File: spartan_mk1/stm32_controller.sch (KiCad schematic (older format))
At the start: 26 parts

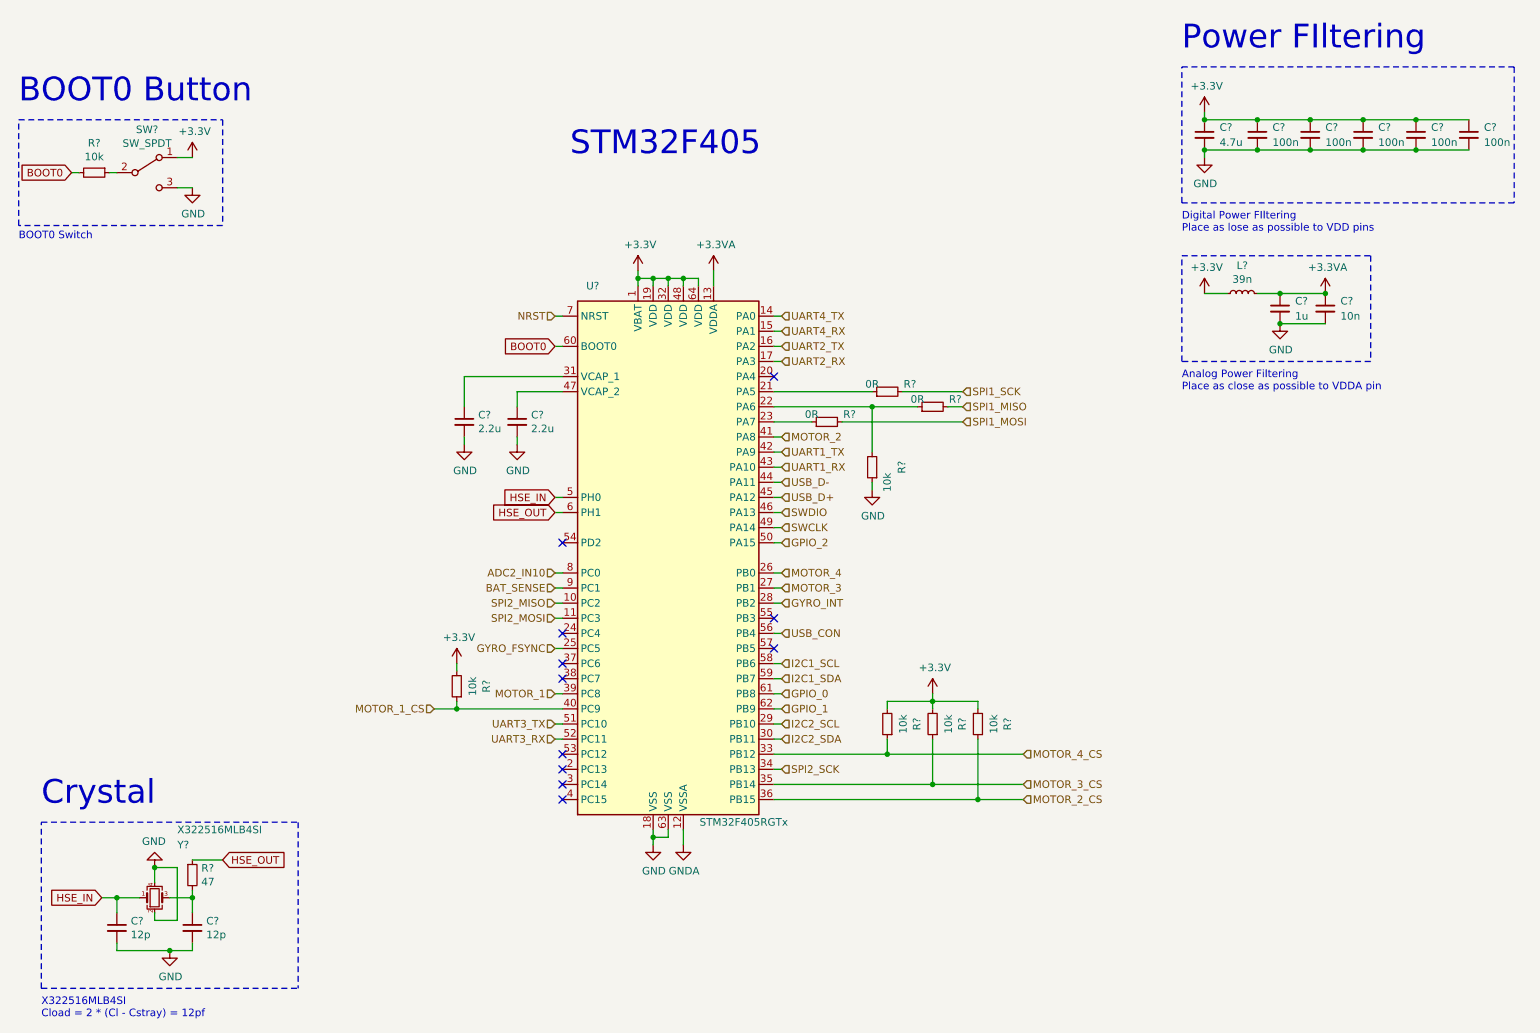
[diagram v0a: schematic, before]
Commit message: Complete schematic with DRC done
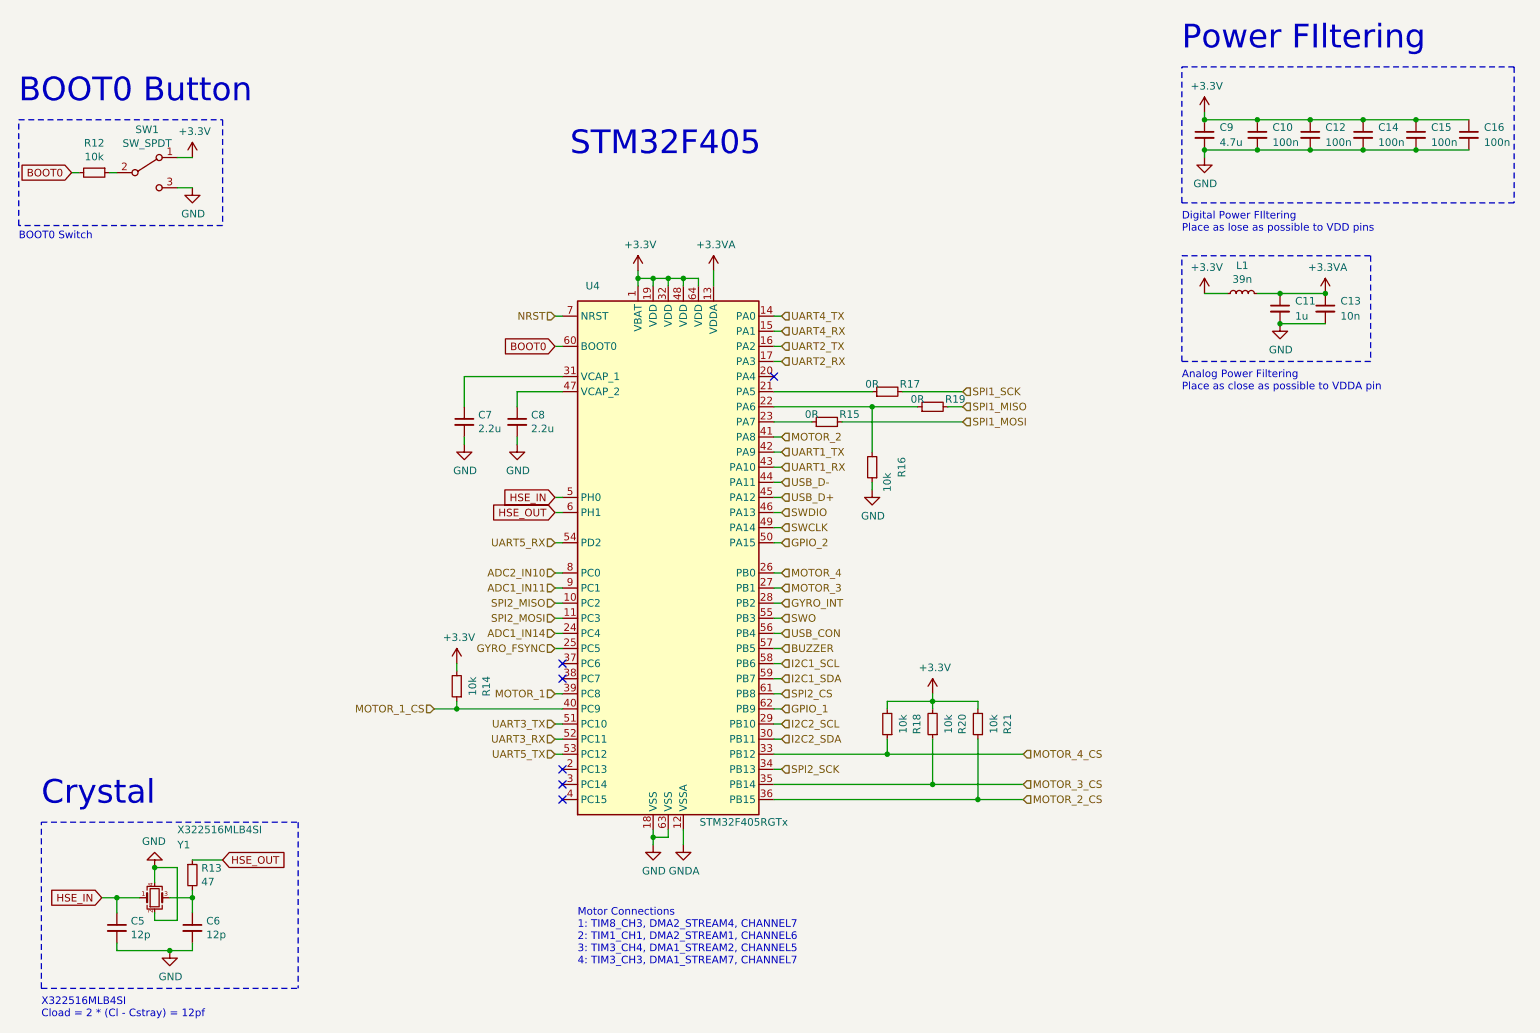
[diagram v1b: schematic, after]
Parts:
- gave numbers to parts that had none: 26
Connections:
- net ADC1_IN14: now reaches U4.24 (PC4)
- net UART5_TX: now reaches U4.53 (PC12)
- net UART5_RX: now reaches U4.54 (PD2)
- net SWO: now reaches U4.55 (PB3)
- net BUZZER: now reaches U4.57 (PB5)
- net BAT_SENSE renamed ADC1_IN11
- net GPIO_0 renamed SPI2_CS
- no-connect marks 11 -> 6
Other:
- note added: "Motor Connections\n1: TIM8_CH3, DMA2_STREAM4, CHANNEL7\n2: TIM1_CH1, DMA2_STREAM1, CHANNEL6\n3: TIM3_CH4, DMA1_STREAM2, CHANNEL5\n4: TIM3_CH3, DMA1_STREAM7, CHANNEL7"

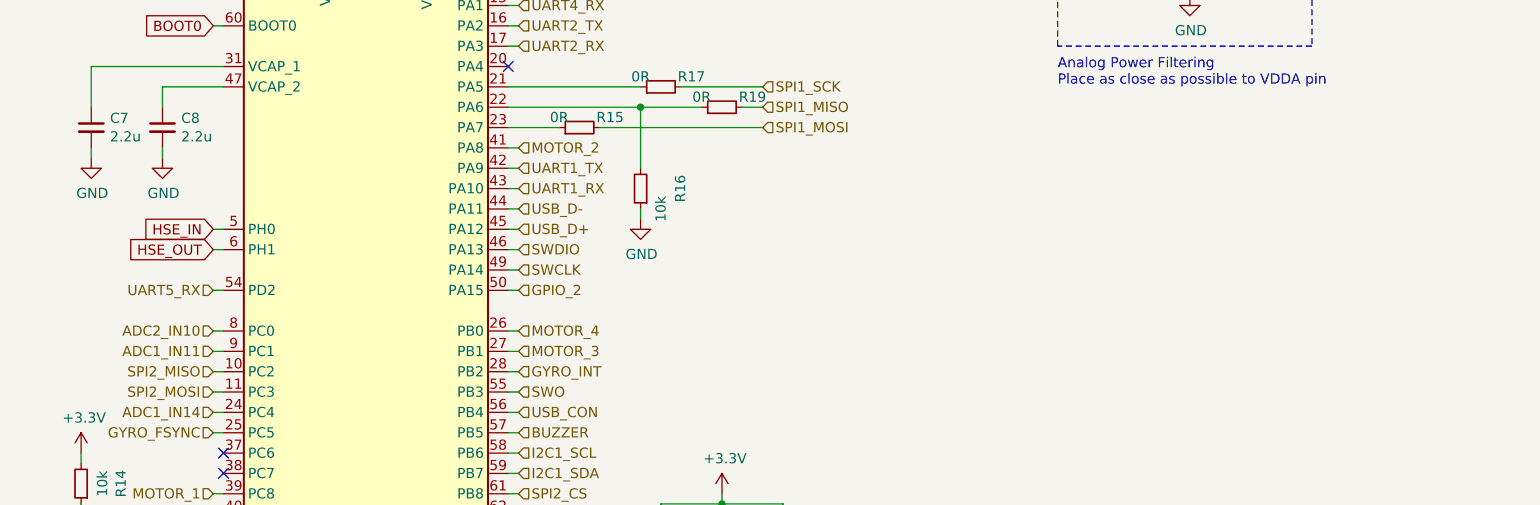
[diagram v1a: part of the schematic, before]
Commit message: Footprints added started PCB placement
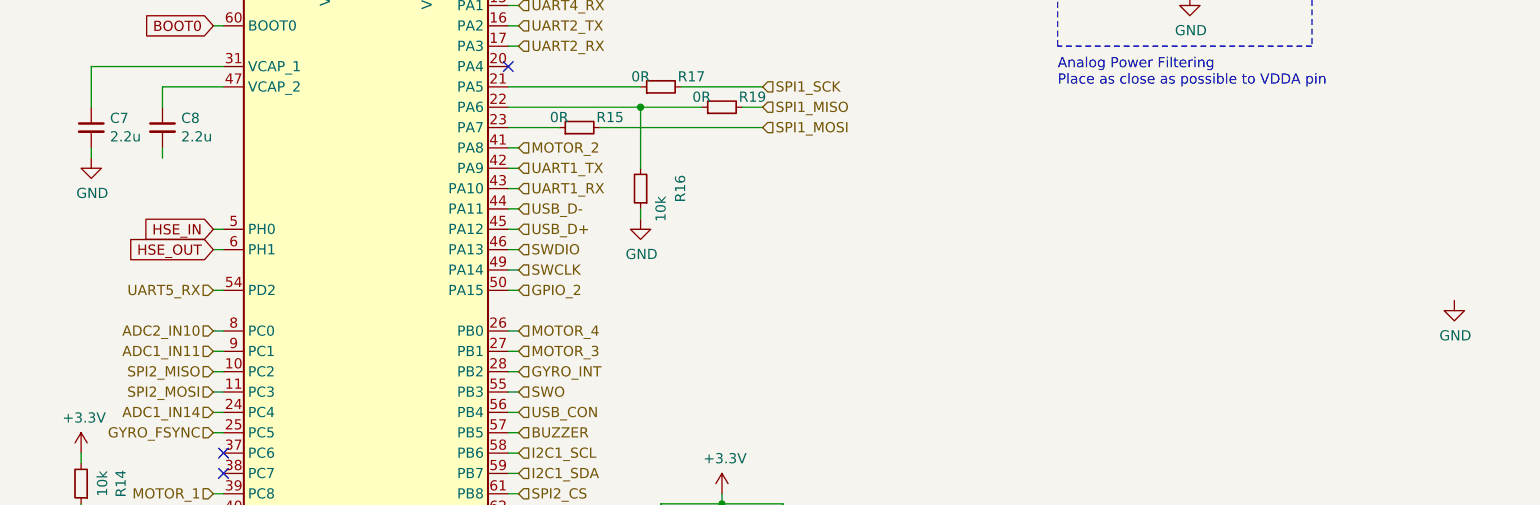
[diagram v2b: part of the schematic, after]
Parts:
- C10, C11, C12, C13, C14, C15, C16, C5, C6, C7, C8, C9: footprint (none) -> Capacitor_SMD:C_0402_1005Metric
- L1: footprint (none) -> Inductor_SMD:L_0402_1005Metric
- R12, R14, R15, R16, R17, R18, R19, R20, R21: footprint (none) -> Resistor_SMD:R_0402_1005Metric
- R13: footprint (none) -> Resistor_SMD:R_0603_1608Metric
- Y1: footprint (none) -> Crystal:Crystal_SMD_3225-4Pin_3.2x2.5mm
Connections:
- net GND: no longer C8.2
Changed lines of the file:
@@
 F 0 "C8" H 4342 3446 50  0000 L CNN
 F 1 "2.2u" H 4342 3355 50  0000 L CNN
-F 2 "" H 4250 3400 50  0001 C CNN
+F 2 "Capacitor_SMD:C_0402_1005Metric" H 4250 3400 50  0001 C CNN
 F 3 "~" H 4250 3400 50  0001 C CNN
 	1    4250 3400
@@
 F 0 "C7" H 3992 3446 50  0000 L CNN
 F 1 "2.2u" H 3992 3355 50  0000 L CNN
-F 2 "" H 3900 3400 50  0001 C CNN
+F 2 "Capacitor_SMD:C_0402_1005Metric" H 3900 3400 50  0001 C CNN
 F 3 "~" H 3900 3400 50  0001 C CNN
 	1    3900 3400
@@
 L power:GND #PWR037
 U 1 1 5F82F59F
-P 4250 3550
-F 0 "#PWR037" H 4250 3300 50  0001 C CNN
-F 1 "GND" H 4255 3377 50  0000 C CNN
-F 2 "" H 4250 3550 50  0001 C CNN
-F 3 "" H 4250 3550 50  0001 C CNN
-	1    4250 3550
+P 10600 4250
+F 0 "#PWR037" H 10600 4000 50  0001 C CNN
+F 1 "GND" H 10605 4077 50  0000 C CNN
+F 2 "" H 10600 4250 50  0001 C CNN
+F 3 "" H 10600 4250 50  0001 C CNN
+	1    10600 4250
 	1    0    0    -1
 $EndComp
@@
 F 0 "R12" V 1254 1750 50  0000 C CNN
 F 1 "10k" V 1345 1750 50  0000 C CNN
-F 2 "" H 1450 1750 50  0001 C CNN
+F 2 "Resistor_SMD:R_0402_1005Metric" H 1450 1750 50  0001 C CNN
 F 3 "~" H 1450 1750 50  0001 C CNN
 	1    1450 1750
@@
 F 0 "C9" H 8900 1550 50  0000 L CNN
 F 1 "4.7u" H 8900 1450 50  0000 L CNN
-F 2 "" H 8800 1500 50  0001 C CNN
+F 2 "Capacitor_SMD:C_0402_1005Metric" H 8800 1500 50  0001 C CNN
 F 3 "~" H 8800 1500 50  0001 C CNN
 	1    8800 1500
@@
 F 0 "C10" H 9250 1550 50  0000 L CNN
 F 1 "100n" H 9250 1450 50  0000 L CNN
-F 2 "" H 9150 1500 50  0001 C CNN
+F 2 "Capacitor_SMD:C_0402_1005Metric" H 9150 1500 50  0001 C CNN
 F 3 "~" H 9150 1500 50  0001 C CNN
 	1    9150 1500
@@
 F 0 "C12" H 9600 1550 50  0000 L CNN
 F 1 "100n" H 9600 1450 50  0000 L CNN
-F 2 "" H 9500 1500 50  0001 C CNN
+F 2 "Capacitor_SMD:C_0402_1005Metric" H 9500 1500 50  0001 C CNN
 F 3 "~" H 9500 1500 50  0001 C CNN
 	1    9500 1500
@@
 F 0 "C14" H 9950 1550 50  0000 L CNN
 F 1 "100n" H 9950 1450 50  0000 L CNN
-F 2 "" H 9850 1500 50  0001 C CNN
+F 2 "Capacitor_SMD:C_0402_1005Metric" H 9850 1500 50  0001 C CNN
 F 3 "~" H 9850 1500 50  0001 C CNN
 	1    9850 1500
@@
 F 0 "C15" H 10300 1550 50  0000 L CNN
 F 1 "100n" H 10300 1450 50  0000 L CNN
-F 2 "" H 10200 1500 50  0001 C CNN
+F 2 "Capacitor_SMD:C_0402_1005Metric" H 10200 1500 50  0001 C CNN
 F 3 "~" H 10200 1500 50  0001 C CNN
 	1    10200 1500
@@
 F 0 "C16" H 10650 1550 50  0000 L CNN
 F 1 "100n" H 10650 1450 50  0000 L CNN
-F 2 "" H 10550 1500 50  0001 C CNN
+F 2 "Capacitor_SMD:C_0402_1005Metric" H 10550 1500 50  0001 C CNN
 F 3 "~" H 10550 1500 50  0001 C CNN
 	1    10550 1500
@@
 F 0 "C11" H 9400 2700 50  0000 L CNN
 F 1 "1u" H 9400 2600 50  0000 L CNN
-F 2 "" H 9300 2650 50  0001 C CNN
+F 2 "Capacitor_SMD:C_0402_1005Metric" H 9300 2650 50  0001 C CNN
 F 3 "~" H 9300 2650 50  0001 C CNN
 	1    9300 2650
@@
 F 0 "C13" H 9700 2700 50  0000 L CNN
 F 1 "10n" H 9700 2600 50  0000 L CNN
-F 2 "" H 9600 2650 50  0001 C CNN
+F 2 "Capacitor_SMD:C_0402_1005Metric" H 9600 2650 50  0001 C CNN
 F 3 "~" H 9600 2650 50  0001 C CNN
 	1    9600 2650
@@
 F 0 "L1" V 9235 2550 50  0000 C CNN
 F 1 "39n" V 9144 2550 50  0000 C CNN
-F 2 "" H 9050 2550 50  0001 C CNN
+F 2 "Inductor_SMD:L_0402_1005Metric" H 9050 2550 50  0001 C CNN
 F 3 "~" H 9050 2550 50  0001 C CNN
 	1    9050 2550
@@
 F 0 "Y1" H 2000 6900 50  0000 L CNN
 F 1 "X322516MLB4SI" H 2000 7000 50  0000 L CNN
-F 2 "" H 1850 6550 50  0001 C CNN
+F 2 "Crystal:Crystal_SMD_3225-4Pin_3.2x2.5mm" H 1850 6550 50  0001 C CNN
 F 3 "~" H 1850 6550 50  0001 C CNN
 	1    1850 6550
@@
 F 0 "C6" H 2192 6796 50  0000 L CNN
 F 1 "12p" H 2192 6705 50  0000 L CNN
-F 2 "" H 2100 6750 50  0001 C CNN
+F 2 "Capacitor_SMD:C_0402_1005Metric" H 2100 6750 50  0001 C CNN
 F 3 "~" H 2100 6750 50  0001 C CNN
 	1    2100 6750
@@
 F 0 "C5" H 1692 6796 50  0000 L CNN
 F 1 "12p" H 1692 6705 50  0000 L CNN
-F 2 "" H 1600 6750 50  0001 C CNN
+F 2 "Capacitor_SMD:C_0402_1005Metric" H 1600 6750 50  0001 C CNN
 F 3 "~" H 1600 6750 50  0001 C CNN
 	1    1600 6750
@@
 F 0 "R13" H 2159 6446 50  0000 L CNN
 F 1 "47" H 2159 6355 50  0000 L CNN
-F 2 "" H 2100 6400 50  0001 C CNN
+F 2 "Resistor_SMD:R_0603_1608Metric" H 2100 6400 50  0001 C CNN
 F 3 "~" H 2100 6400 50  0001 C CNN
 	1    2100 6400
@@
 F 0 "R18" V 6504 5400 50  0000 C CNN
 F 1 "10k" V 6595 5400 50  0000 C CNN
-F 2 "" H 6700 5400 50  0001 C CNN
+F 2 "Resistor_SMD:R_0402_1005Metric" H 6700 5400 50  0001 C CNN
 F 3 "~" H 6700 5400 50  0001 C CNN
 	1    6700 5400
@@
 F 0 "R20" V 6804 5400 50  0000 C CNN
 F 1 "10k" V 6895 5400 50  0000 C CNN
-F 2 "" H 7000 5400 50  0001 C CNN
+F 2 "Resistor_SMD:R_0402_1005Metric" H 7000 5400 50  0001 C CNN
 F 3 "~" H 7000 5400 50  0001 C CNN
 	1    7000 5400
@@
 F 0 "R21" V 7104 5400 50  0000 C CNN
 F 1 "10k" V 7195 5400 50  0000 C CNN
-F 2 "" H 7300 5400 50  0001 C CNN
+F 2 "Resistor_SMD:R_0402_1005Metric" H 7300 5400 50  0001 C CNN
 F 3 "~" H 7300 5400 50  0001 C CNN
 	1    7300 5400
@@
 F 0 "R14" V 3654 5150 50  0000 C CNN
 F 1 "10k" V 3745 5150 50  0000 C CNN
-F 2 "" H 3850 5150 50  0001 C CNN
+F 2 "Resistor_SMD:R_0402_1005Metric" H 3850 5150 50  0001 C CNN
 F 3 "~" H 3850 5150 50  0001 C CNN
 	1    3850 5150
@@
 F 0 "R16" V 6404 3700 50  0000 C CNN
 F 1 "10k" V 6500 3800 50  0000 C CNN
-F 2 "" H 6600 3700 50  0001 C CNN
+F 2 "Resistor_SMD:R_0402_1005Metric" H 6600 3700 50  0001 C CNN
 F 3 "~" H 6600 3700 50  0001 C CNN
 	1    6600 3700
@@
 F 0 "R19" V 7050 3150 50  0000 C CNN
 F 1 "0R" V 7050 3400 50  0000 C CNN
-F 2 "" H 7000 3300 50  0001 C CNN
+F 2 "Resistor_SMD:R_0402_1005Metric" H 7000 3300 50  0001 C CNN
 F 3 "~" H 7000 3300 50  0001 C CNN
 	1    7000 3300
@@
 F 0 "R17" V 6750 3050 50  0000 C CNN
 F 1 "0R" V 6750 3300 50  0000 C CNN
-F 2 "" H 6700 3200 50  0001 C CNN
+F 2 "Resistor_SMD:R_0402_1005Metric" H 6700 3200 50  0001 C CNN
 F 3 "~" H 6700 3200 50  0001 C CNN
 	1    6700 3200
@@
 F 0 "R15" V 6350 3250 50  0000 C CNN
 F 1 "0R" V 6350 3500 50  0000 C CNN
-F 2 "" H 6300 3400 50  0001 C CNN
+F 2 "Resistor_SMD:R_0402_1005Metric" H 6300 3400 50  0001 C CNN
 F 3 "~" H 6300 3400 50  0001 C CNN
 	1    6300 3400
